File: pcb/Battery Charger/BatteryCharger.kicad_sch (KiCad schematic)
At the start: 15 parts, among them U2 MCP73831-2-OT, U3 MCP73831-2-OT

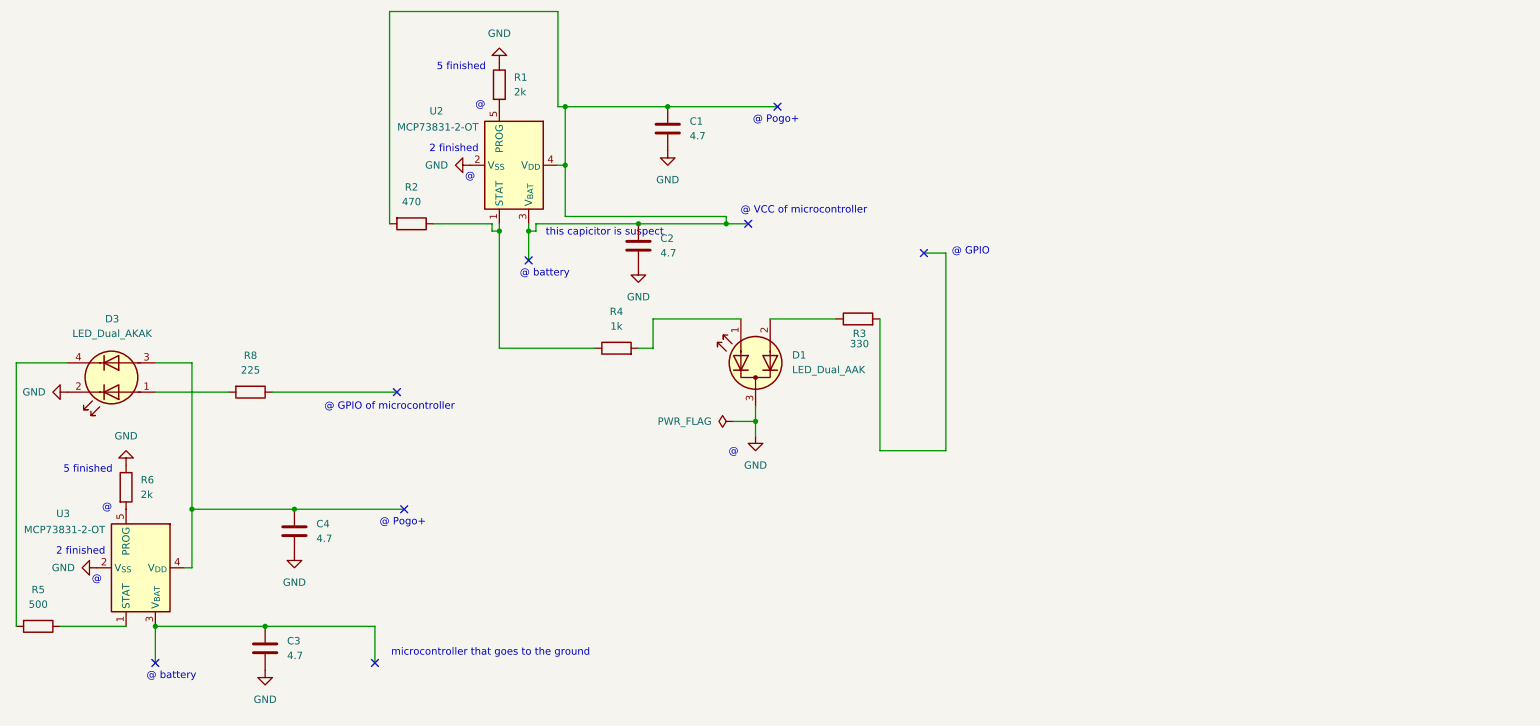
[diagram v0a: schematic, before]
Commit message: I added the 2 extra components to the battery regulator
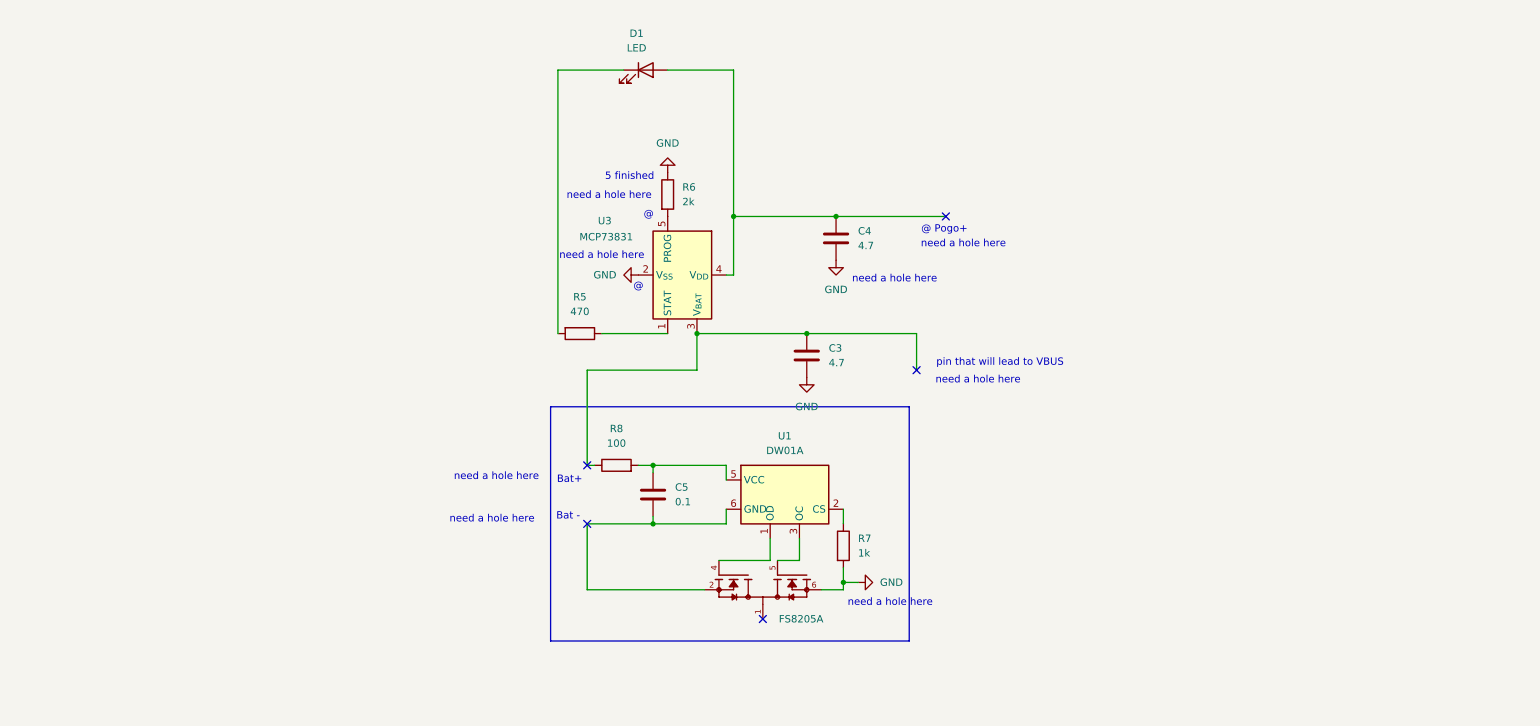
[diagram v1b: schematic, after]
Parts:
- removed C1, C2: 4.7, symbol Device:C
- removed D1: LED_Dual_AAK, LED_SMD:LED-L1T2_LUMILEDS, symbol Device:LED_Dual_AAK
- removed D3: LED_Dual_AKAK, symbol Device:LED_Dual_AKAK
- removed R1: 2k, Resistor_SMD:R_0603_1608Metric, symbol Device:R
- removed R2: 470, Resistor_SMD:R_0603_1608Metric, symbol Device:R
- removed R3: 330, Resistor_SMD:R_0603_1608Metric, symbol Device:R
- removed R4: 1k, Resistor_SMD:R_0603_1608Metric, symbol Device:R
- removed U2: MCP73831-2-OT, Package_TO_SOT_SMD:SOT-23-5, symbol Battery_Management:MCP73831-2-OT
- added C5: 0.1, symbol Device:C
- added D1: LED, symbol Device:LED
- added Q1: FS8205A, symbol FS8205:FS8205A
- added R7: 1k, Resistor_SMD:R_0603_1608Metric, symbol Device:R
- added U1: DW01A, Package_TO_SOT_SMD:SOT-23-6, symbol Battery_Management:DW01A
- R5: value 500 -> 470
- R8: value 225 -> 100
- U3: value MCP73831-2-OT -> MCP73831
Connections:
- net GND: now also Q1.6, Q1.7, R7.2
- net at R8.1: now also C3.1, U3.3 (V_{BAT})
- net at R8.2: now also C5.1, U1.5 (VCC)
- net at C4.1, U3.4 (V_{DD}): now also D1.2 (A)
- net at R5.2: now also D1.1 (K)
- new net: Q1.4, U1.1 (OD)
- new net: R7.1, U1.2 (CS)
- new net: Q1.5, U1.3 (OC)
- new net: C5.2, Q1.2, Q1.3, U1.6 (GND)
- no-connect marks 8 -> 5
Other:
- note added: "Bat -"
- note added: "Bat+"
- note added: "need a hole here"
- note added: "pin that will lead to VBUS"
- note removed: "2 finished"
- note removed: "@ GPIO"
- note removed: "@ GPIO of microcontroller"
- note removed: "@ VCC of microcontroller"
- note removed: "@ battery"
- note removed: "microcontroller that goes to the ground"
- note removed: "this capicitor is suspect"
- moved on the sheet: C3, C4, R5, R6, U3

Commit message: type shiii
I added the booster converter
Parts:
- added BT1: Battery, symbol Device:Battery
- added C1, C2: 12, symbol Device:C
- added D2, D3: SS14, Diode_SMD:D_SMA, symbol Diode:SS14
- added L1: 22, symbol Device:L
- added PS1: ME2108A33P, symbol FS8205:ME2108A33P
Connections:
- net GND: now also Q1.1, PS1.4 (GND); no longer Q1.6, Q1.7, R7.2
- net at C4.1, D1.2 (A), U3.4 (V_{DD}): now also D3.1 (K)
- net at C5.2, Q1.2, Q1.3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: now also BT1.2 (-)
- net at C3.1, U3.3 (V_{BAT}): now also C1.1, C2.1, D2.1 (K), D3.2 (A), PS1.2 (VOUT); no longer R8.1
- new net: C1.2, C2.2, PS1.1 (VSS), Q1.6, Q1.7, R7.2
- new net: D2.2 (A), L1.2, PS1.3 (LX)
- new net: BT1.1 (+), L1.1, R8.1
- no-connect marks 5 -> 3
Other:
- note added: "uh bat -"
- moved on the sheet: C3, C4, C5, R7, R8, U1

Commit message: i just made some changes
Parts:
- removed BT1: Battery, symbol Device:Battery
- added B+1: B+, symbol Connector:TestPoint
- added B-1, GND1: B-, symbol Connector:TestPoint
- added D4, D5: SS14, Diode_SMD:D_SMA, symbol Diode:SS14
- added Pogo+1: Pogo+, symbol Connector:TestPoint
- added VBUS1: Output 5V, symbol Connector:TestPoint
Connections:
- net GND: now also C1.2, C2.2, PS1.1 (VSS), Q1.6, Q1.7, R7.2, GND1.1; no longer Q1.1
- net at C1.1, C2.1, C3.1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: now also D4.1 (K); no longer U3.3 (V_{BAT})
- net at C4.1, D1.2 (A), U3.4 (V_{DD}): now also D5.2 (A), Pogo+1.1; no longer D3.1 (K)
- net at L1.1, R8.1: now also U3.3 (V_{BAT}), B+1.1, D4.2 (A)
- net at C5.2, Q1.2, Q1.3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: now also B-1.1
- new net: D3.1 (K), D5.1 (K), VBUS1.1
- no-connect marks 3 -> 2
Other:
- note added: "this end should be able to be untethered"
- note added: "this segment should just output 5v"
- moved on the sheet: C3, D3, L1, R8

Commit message: Rough Draft FINISHED
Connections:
- no-connect marks 2 -> 1
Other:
- note added: "Bat-"
- note added: "Boost Converter that changes 3.7V to 5V"
- note added: "Regulates 5V from Pogo and lights up when charging"
- note removed: "5 finished"
- note removed: "@"
- note removed: "@ Pogo+"
- note removed: "Bat -"
- note removed: "pin that will lead to VBUS"
- note removed: "this end should be able to be untethered"
- note removed: "uh bat -"
- moved on the sheet: D1, R6, VBUS1
